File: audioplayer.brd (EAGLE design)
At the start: 53.3 x 53.3 mm, 28 parts, among them J1 MICRO-SDCARD-CONNECTOR-330006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, J10 CONNECTOR-HEADER-8P-3460290P1, J11 CONNECTOR-HEADER-8P-3460290P1, J2 JST-2P-SMD-PW-3410050P1, J3 MICRO-USB-5P-340015001, J4 CONNECTOR-HEADER-2X3P-3460180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, J5 AUDIO-CONNECTOR-6P-SMD-344003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, J6 SCREW-TERMINAL-2P-3470070P1, J7 CONNECTOR-HEADER-6P-3460650P1, J8 CONNECTOR-HEADER-6P-3460270P1, J9 CONNECTOR-HEADER-10P-3460170P1, K1 BUTTON-4P-3100010P1, U1 ATMEGA328P-AU-1030060P1, U2 CN3065-1320040P1, U3 XC6206-3.3-1300260P1, X1 CRYSTAL-0500290P1

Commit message: 1.5 hrs: routing.
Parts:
- C3, C4: value (none) -> 22pF
- R1: value (none) -> 4.7K
- moved C10 15.2 mm to (22.9, 19.1)
- moved R1 7.08 mm to (28.1, 41.9), turned to 270 degrees
- moved C2 3.95 mm to (48.0, 40.9)
- moved C6 2.84 mm to (36.8, 39.4)
- moved C7 2.84 mm to (36.8, 36.8)
- moved U2 2.84 mm to (31.8, 40.6), turned to 0 degrees
- moved C9 2.54 mm to (35.6, 25.4)
- moved U3 2.54 mm to (31.8, 25.4)
- moved C5 2.54 mm to (24.1, 40.6)
- moved C8 2.54 mm to (31.8, 21.6)
- moved J5 1.52 mm to (65.0, 10.2)
- moved K1 1.02 mm to (25.4, 11.7)
- moved R2 0.80 mm to (31.0, 16.3), turned to 270 degrees
- moved J3 0.76 mm to (17.0, 40.6)
- moved C1 0.57 mm to (37.8, 23.1)
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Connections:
- new net VFTDI: J7.3
- net 3V3: no longer J7.3
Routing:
- net RESET: track 0.00 -> 77.2 mm
- net 3V3: track 0.00 -> 76.5 mm
- net MOSI: track 0.00 -> 46.3 mm, vias 0 -> 2
- net SCK: track 0.00 -> 39.1 mm, vias 0 -> 2
- net TX: track 0.00 -> 37.5 mm
- net VBAT: track 0.00 -> 33.6 mm
- net MISO: track 0.00 -> 30.8 mm
- net RX: track 0.00 -> 30.3 mm
- net SS: track 0.00 -> 22.1 mm, vias 0 -> 2
- net 5V: track 0.00 -> 13.3 mm
- net DTR: track 0.00 -> 4.10 mm
- net N$1: track 0.00 -> 2.54 mm
- net N$2: track 0.00 -> 2.46 mm
- added copper zone on layer 1, net GND
- added copper zone on layer 16, net GND

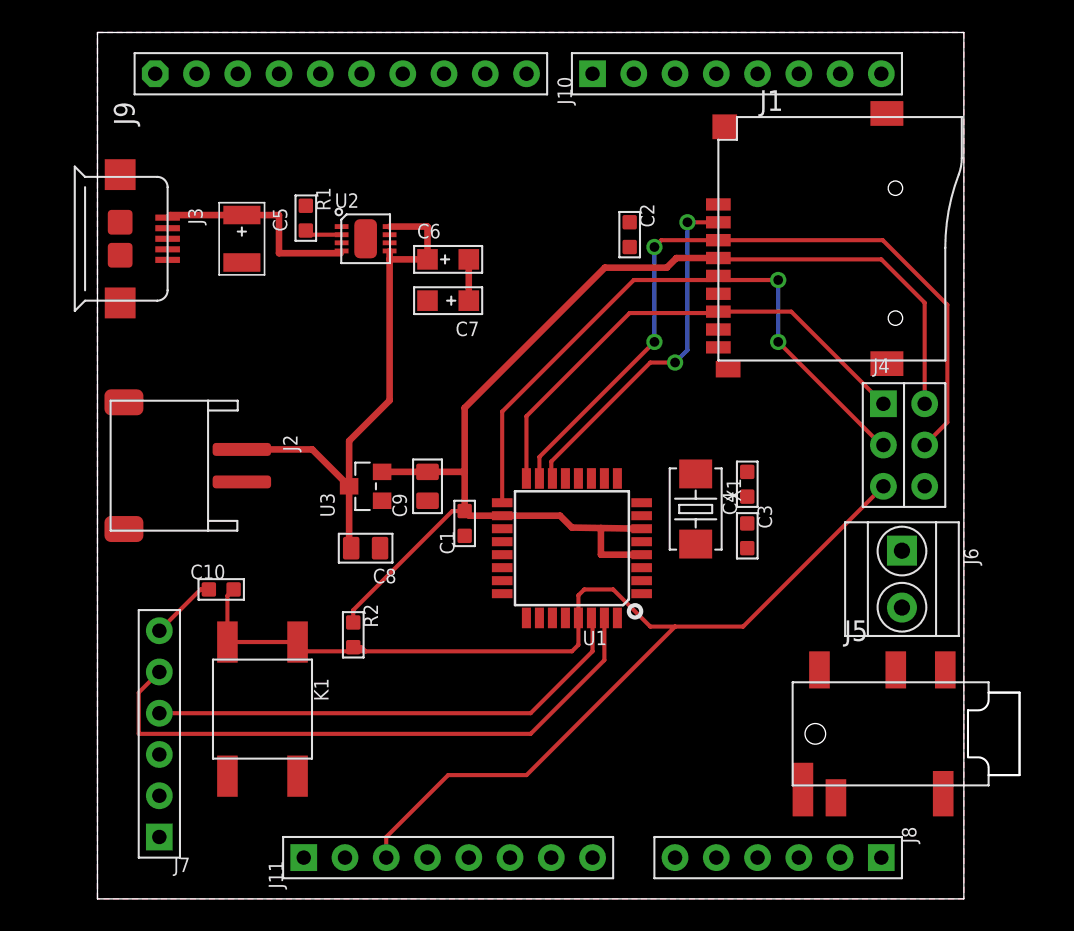
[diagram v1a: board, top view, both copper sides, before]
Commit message: 2 hrs. Routing the rest of the traces. Fix reset button.
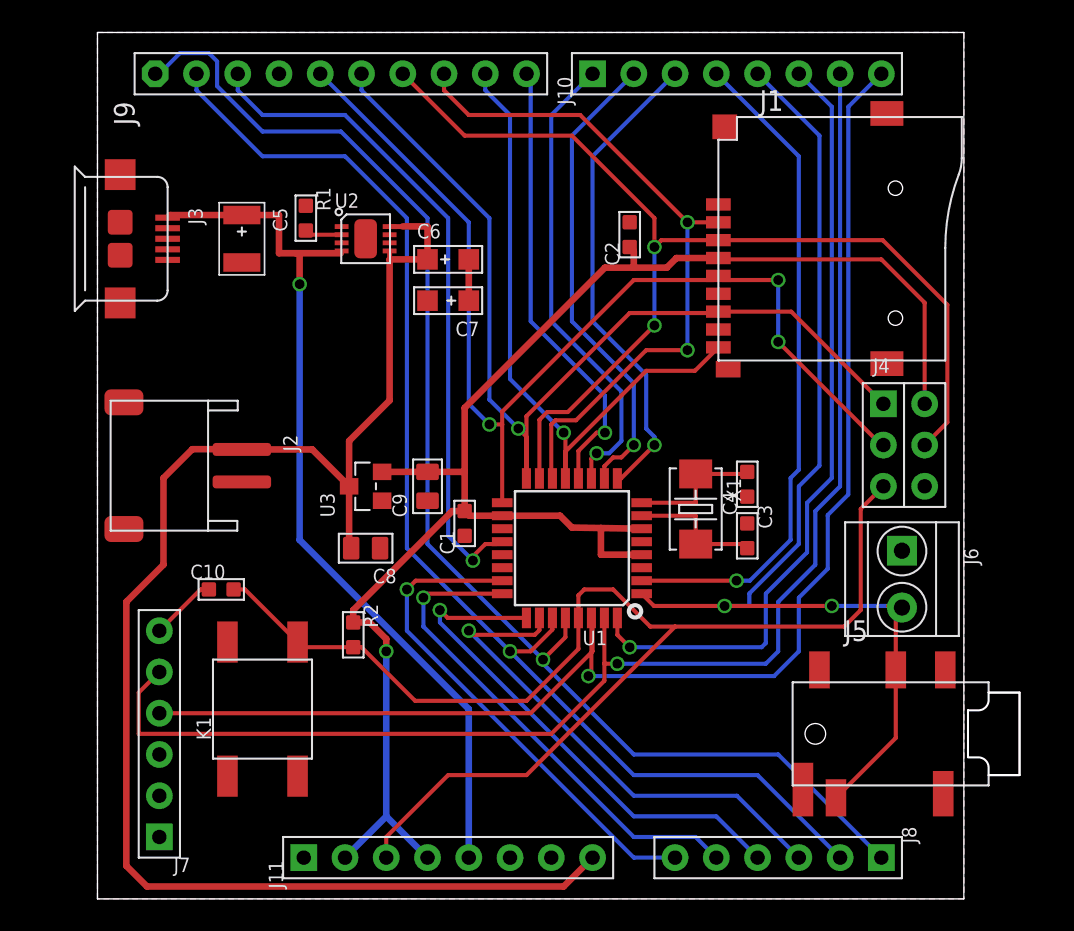
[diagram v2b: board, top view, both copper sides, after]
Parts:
- turned C2 to 90 degrees
- turned K1 to 90 degrees
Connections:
- net GND: now also K1.0A; no longer K1.0B, K1.1B
- net RESET: now also K1.1B; no longer K1.0A, K1.1A
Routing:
- net SCL: track 0.00 -> 81.7 mm, vias 0 -> 1
- net SDA: track 0.00 -> 76.0 mm, vias 0 -> 1
- net AUDIO: track 0.00 -> 68.2 mm, vias 0 -> 2
- net VBAT: track 33.6 -> 94.0 mm
- net RX: track 30.3 -> 85.2 mm, vias 0 -> 1
- net TX: track 37.5 -> 86.4 mm, vias 0 -> 1
- net N$15: track 0.00 -> 48.2 mm, vias 0 -> 1
- net 5V: track 13.3 -> 54.9 mm, vias 0 -> 1
- net AREF: track 0.00 -> 41.3 mm, vias 0 -> 1
- net N$14: track 0.00 -> 41.2 mm, vias 0 -> 1
- net CDN: track 0.00 -> 40.7 mm, vias 0 -> 1
- net N$7: track 0.00 -> 31.8 mm, vias 0 -> 1
- net N$6: track 0.00 -> 31.4 mm, vias 0 -> 1
- net N$9: track 0.00 -> 30.9 mm, vias 0 -> 1
- net N$8: track 0.00 -> 30.7 mm, vias 0 -> 1
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
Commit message: 0.5 hrs: extend outline, add drill holes, adjust traces and components.
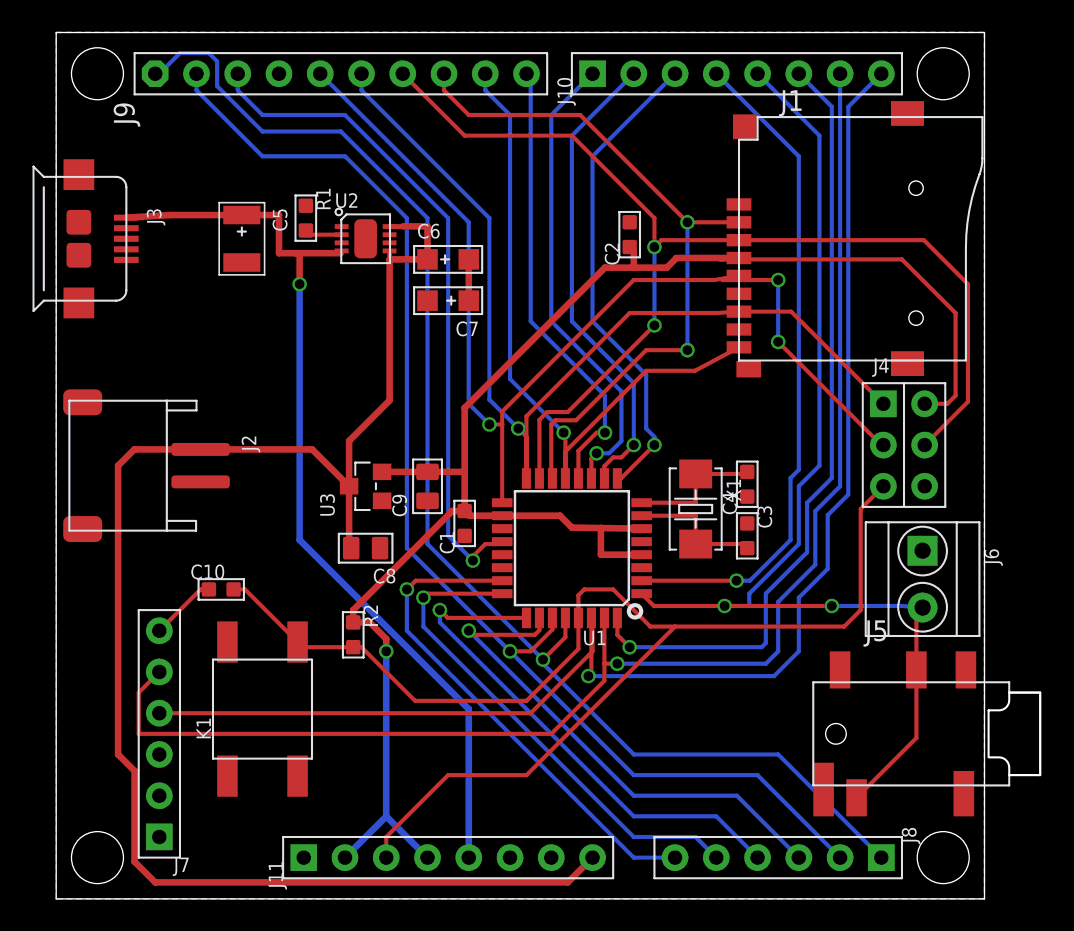
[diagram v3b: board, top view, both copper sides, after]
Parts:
- moved J3 2.54 mm to (14.5, 40.6)
- moved J2 2.54 mm to (16.5, 26.7)
- moved J6 1.27 mm to (66.0, 19.7)
- moved J1 1.27 mm to (62.2, 40.6)
- moved J5 1.27 mm to (66.3, 10.2)
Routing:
- net 3V3: track 98.5 -> 104.0 mm
- net MOSI: track 68.0 -> 70.5 mm
- net 5V: track 54.9 -> 57.4 mm
- net SCK: track 65.8 -> 67.6 mm
- net VBAT: track 94.0 -> 95.8 mm
- net SS: track 42.8 -> 44.1 mm
- net CDN: track 40.7 -> 41.7 mm
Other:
- board size 53.3 x 53.3 mm -> 57.1 x 53.3 mm

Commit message: 0.25 hours: silkscreen and move FTDI header.
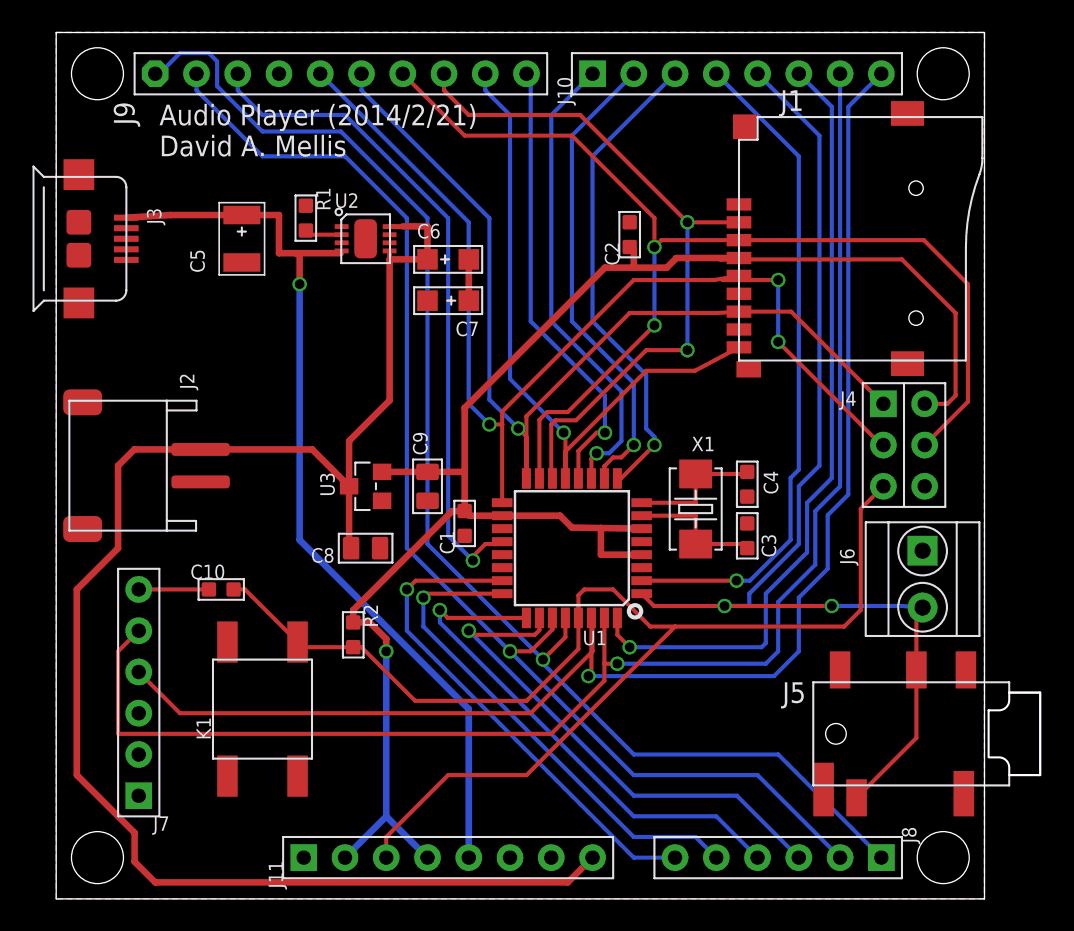
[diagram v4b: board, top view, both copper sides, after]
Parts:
- moved J7 2.84 mm to (17.8, 12.7)
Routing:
- net TX: track 86.4 -> 90.2 mm
- net RX: track 85.2 -> 87.6 mm
- net VBAT: track 95.8 -> 97.9 mm
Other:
- board text added: "Audio Player (2014/2/21) David A. Mellis"

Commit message: 0.5 hrs: improve trace and via spacing, move ATmega capacitor, update date.
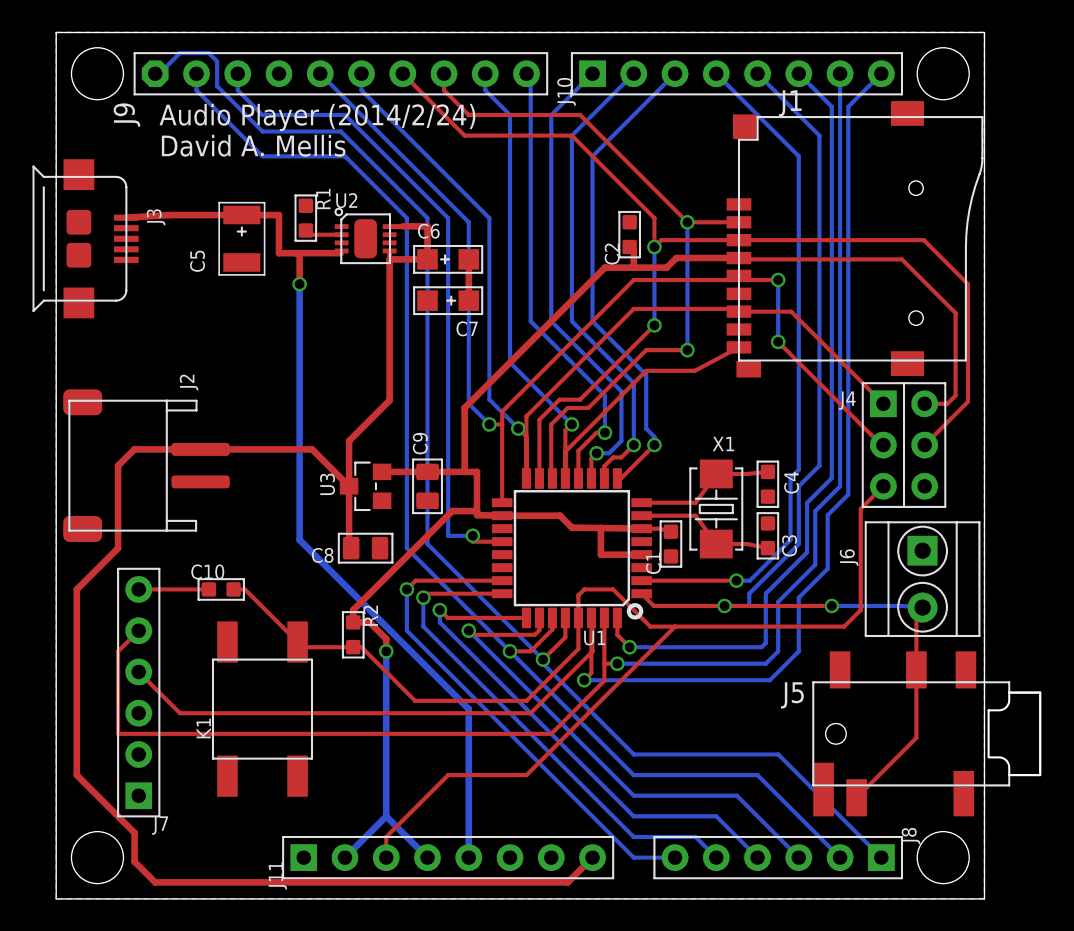
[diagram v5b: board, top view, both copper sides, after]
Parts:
- moved C1 12.8 mm to (50.5, 21.8)
- moved C3 1.27 mm to (56.5, 22.4)
- moved C4 1.27 mm to (56.5, 25.5)
- moved X1 1.27 mm to (53.3, 24.0)
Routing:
- net SCK: track 67.6 -> 65.8 mm
- net AREF: track 41.3 -> 40.5 mm
- net RX: track 87.6 -> 88.3 mm
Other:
- board text added: "Audio Player (2014/2/24) David A. Mellis"
- board text removed: "Audio Player (2014/2/21) David A. Mellis"
